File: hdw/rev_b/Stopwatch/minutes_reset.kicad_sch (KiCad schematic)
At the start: 21 parts

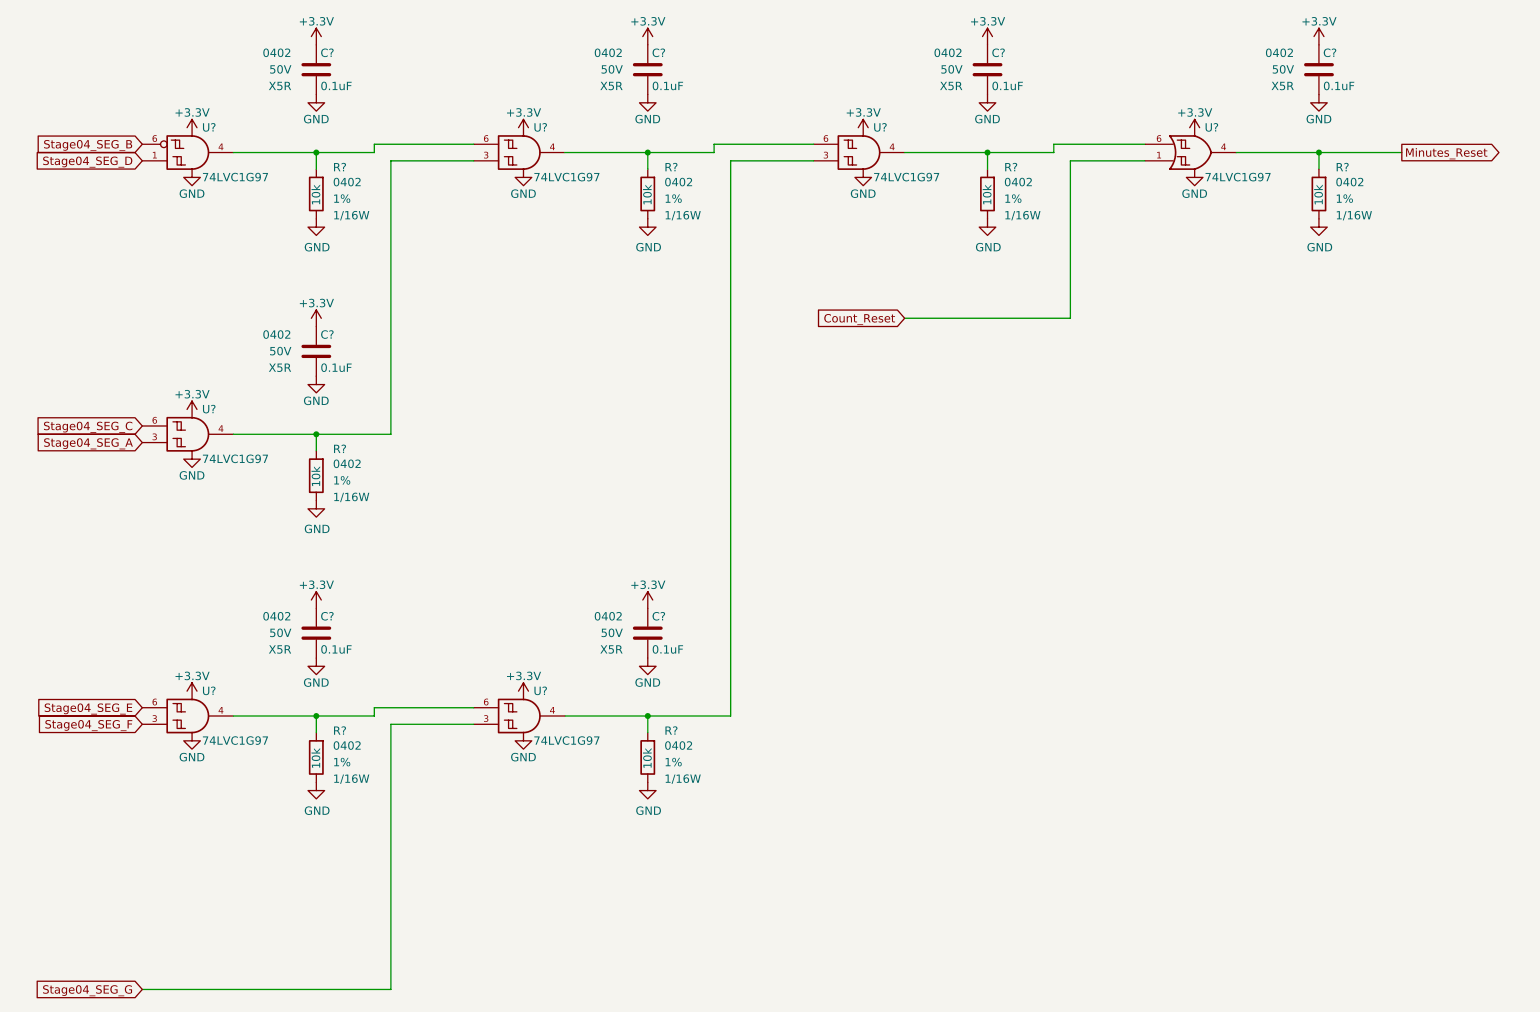
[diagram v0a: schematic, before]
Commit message: ported rev b to kicad 8
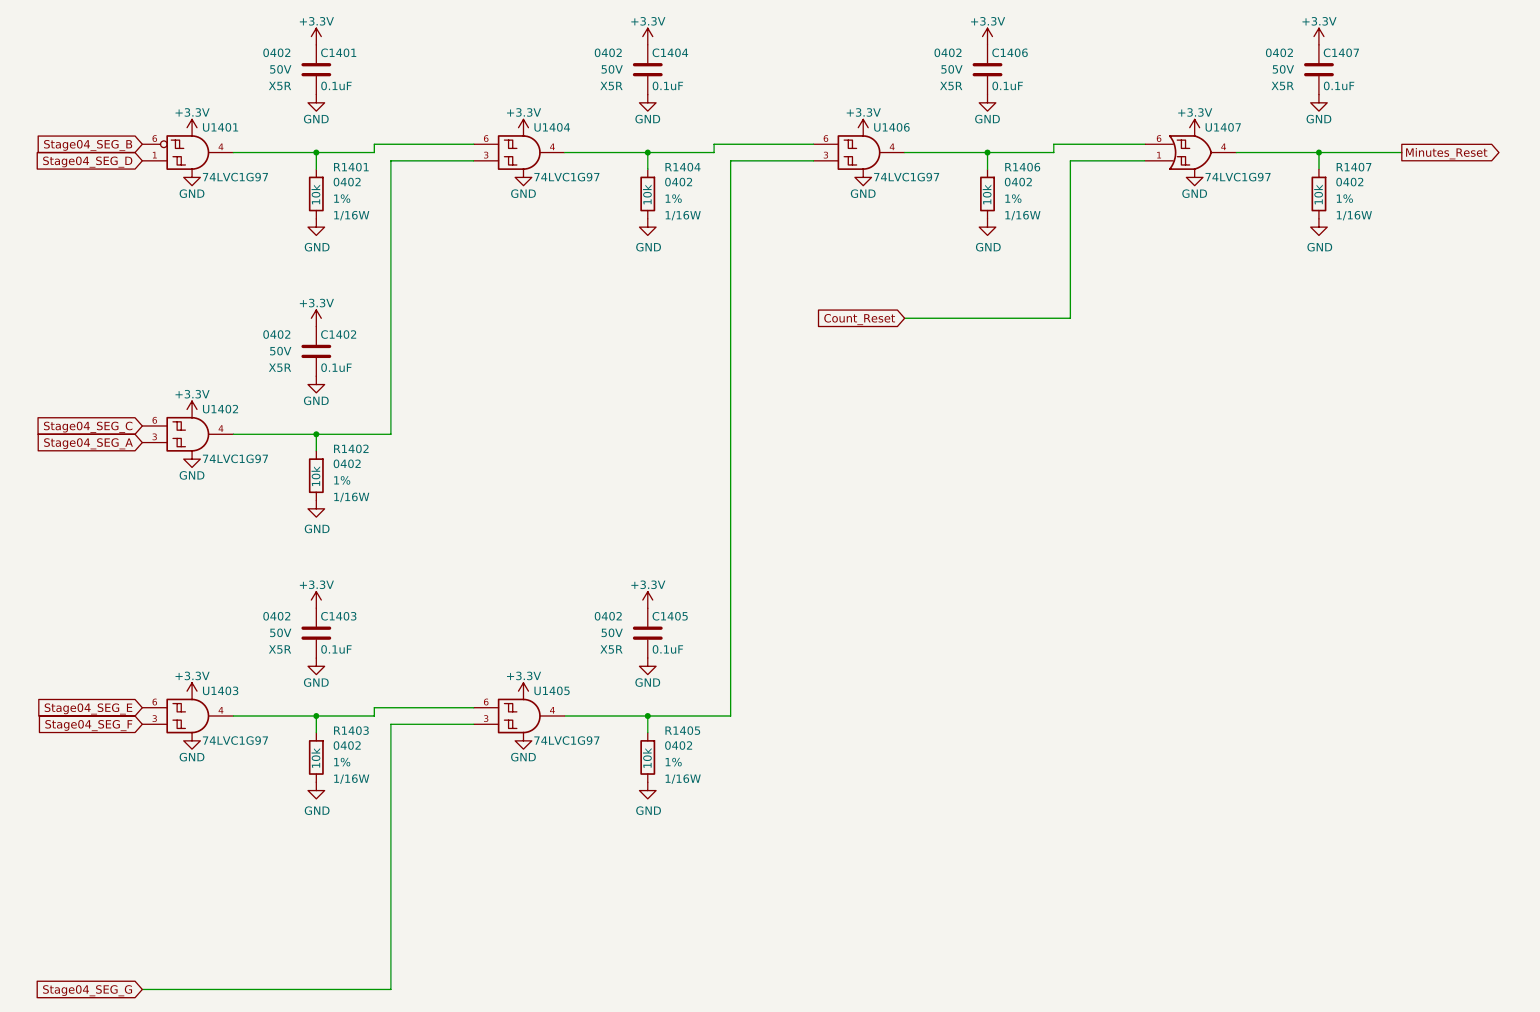
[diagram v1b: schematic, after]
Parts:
- gave numbers to parts that had none: 21

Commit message: integrated SC70 gates
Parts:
- U1401, U1402, U1403, U1404, U1405, U1406, U1407: footprint Package_SON:Fairchild_MicroPak2-6_1.0x1.0mm_P0.35mm -> Package_TO_SOT_SMD:SOT-363_SC-70-6; Digi-Key PN 296-29875-1-ND -> 296-15582-1-ND
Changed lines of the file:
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@@
 			)
 		)
-		(property "Footprint" "Package_SON:Fairchild_MicroPak2-6_1.0x1.0mm_P0.35mm"
+		(property "Footprint" "Package_TO_SOT_SMD:SOT-363_SC-70-6"
 			(at 205.74 39.37 0)
 			(effects
@@
 			)
 		)
-		(property "Digi-Key PN" "296-29875-1-ND"
+		(property "Digi-Key PN" "296-15582-1-ND"
 			(at 204.47 39.37 0)
 			(effects
@@
 			)
 		)
-		(property "Footprint" "Package_SON:Fairchild_MicroPak2-6_1.0x1.0mm_P0.35mm"
+		(property "Footprint" "Package_TO_SOT_SMD:SOT-363_SC-70-6"
 			(at 52.07 82.55 0)
 			(effects
@@
 			)
 		)
-		(property "Digi-Key PN" "296-29875-1-ND"
+		(property "Digi-Key PN" "296-15582-1-ND"
 			(at 50.8 82.55 0)
 			(effects
@@
 			)
 		)
-		(property "Footprint" "Package_SON:Fairchild_MicroPak2-6_1.0x1.0mm_P0.35mm"
+		(property "Footprint" "Package_TO_SOT_SMD:SOT-363_SC-70-6"
 			(at 102.87 125.73 0)
 			(effects
@@
 			)
 		)
-		(property "Digi-Key PN" "296-29875-1-ND"
+		(property "Digi-Key PN" "296-15582-1-ND"
 			(at 101.6 125.73 0)
 			(effects
@@
 			)
 		)
-		(property "Footprint" "Package_SON:Fairchild_MicroPak2-6_1.0x1.0mm_P0.35mm"
+		(property "Footprint" "Package_TO_SOT_SMD:SOT-363_SC-70-6"
 			(at 52.07 39.37 0)
 			(effects
@@
 			)
 		)
-		(property "Digi-Key PN" "296-29875-1-ND"
+		(property "Digi-Key PN" "296-15582-1-ND"
 			(at 50.8 39.37 0)
 			(effects
@@
 			)
 		)
-		(property "Footprint" "Package_SON:Fairchild_MicroPak2-6_1.0x1.0mm_P0.35mm"
+		(property "Footprint" "Package_TO_SOT_SMD:SOT-363_SC-70-6"
 			(at 102.87 39.37 0)
 			(effects
@@
 			)
 		)
-		(property "Digi-Key PN" "296-29875-1-ND"
+		(property "Digi-Key PN" "296-15582-1-ND"
 			(at 101.6 39.37 0)
 			(effects
@@
 			)
 		)
-		(property "Footprint" "Package_SON:Fairchild_MicroPak2-6_1.0x1.0mm_P0.35mm"
+		(property "Footprint" "Package_TO_SOT_SMD:SOT-363_SC-70-6"
 			(at 52.07 125.73 0)
 			(effects
@@
 			)
 		)
-		(property "Digi-Key PN" "296-29875-1-ND"
+		(property "Digi-Key PN" "296-15582-1-ND"
 			(at 50.8 125.73 0)
 			(effects
@@
 			)
 		)
-		(property "Footprint" "Package_SON:Fairchild_MicroPak2-6_1.0x1.0mm_P0.35mm"
+		(property "Footprint" "Package_TO_SOT_SMD:SOT-363_SC-70-6"
 			(at 154.94 39.37 0)
 			(effects
@@
 			)
 		)
-		(property "Digi-Key PN" "296-29875-1-ND"
+		(property "Digi-Key PN" "296-15582-1-ND"
 			(at 153.67 39.37 0)
 			(effects
